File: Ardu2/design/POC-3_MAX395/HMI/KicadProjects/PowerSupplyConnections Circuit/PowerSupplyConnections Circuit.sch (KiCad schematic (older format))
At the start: 16 parts, among them P1 GND, P2 GND, P3 Wiper, P4 Wiper, P5 3.3v, P6 5v

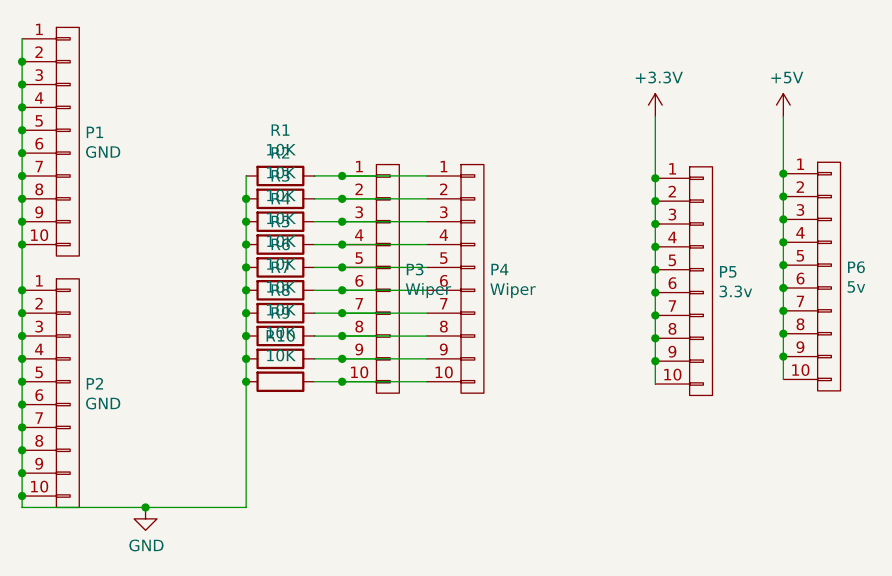
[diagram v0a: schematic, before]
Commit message: created a new peripherals PCB
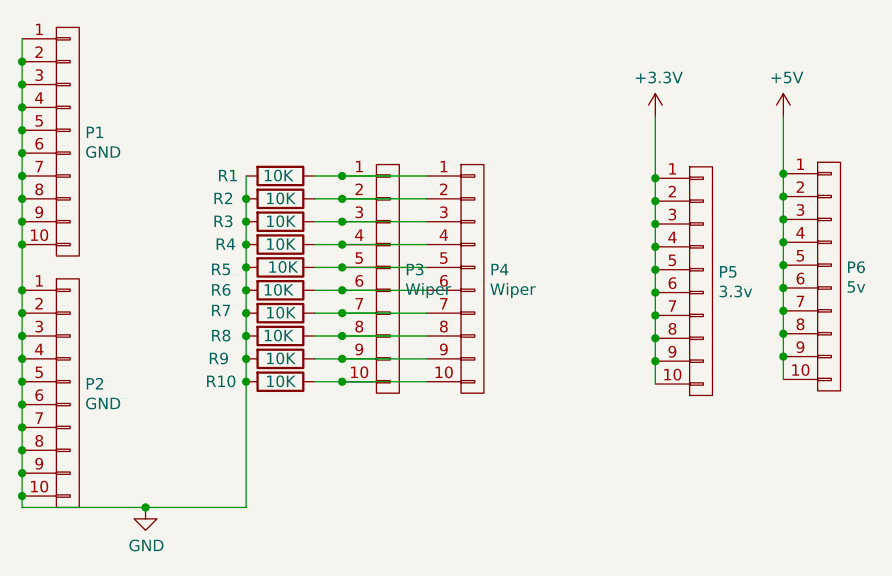
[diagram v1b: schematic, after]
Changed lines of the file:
@@
 LIBS:contrib
 LIBS:valves
+LIBS:PowerSupplyConnections Circuit-cache
 EELAYER 25 0
 EELAYER END
@@
 U 1 1 574B59D1
 P 3570 2660
-F 0 "R1" V 3371 2660 50  0000 C CNN
-F 1 "10K" V 3457 2660 50  0000 C CNN
+F 0 "R1" V 3570 2430 50  0000 C CNN
+F 1 "10K" V 3570 2650 50  0000 C CNN
 F 2 "Resistors_ThroughHole:Resistor_Horizontal_RM10mm" V 3500 2660 50  0001 C CNN
 F 3 "" H 3570 2660 50  0000 C CNN
@@
 U 1 1 574B5BBD
 P 3570 2760
-F 0 "R2" V 3371 2760 50  0000 C CNN
-F 1 "10K" V 3457 2760 50  0000 C CNN
+F 0 "R2" V 3570 2510 50  0000 C CNN
+F 1 "10K" V 3570 2760 50  0000 C CNN
 F 2 "Resistors_ThroughHole:Resistor_Horizontal_RM10mm" V 3500 2760 50  0001 C CNN
 F 3 "" H 3570 2760 50  0000 C CNN
@@
 U 1 1 574B5C0B
 P 3570 2860
-F 0 "R3" V 3371 2860 50  0000 C CNN
-F 1 "10K" V 3457 2860 50  0000 C CNN
+F 0 "R3" V 3570 2610 50  0000 C CNN
+F 1 "10K" V 3570 2860 50  0000 C CNN
 F 2 "Resistors_ThroughHole:Resistor_Horizontal_RM10mm" V 3500 2860 50  0001 C CNN
 F 3 "" H 3570 2860 50  0000 C CNN
@@
 U 1 1 574B5E4B
 P 3570 2960
-F 0 "R4" V 3371 2960 50  0000 C CNN
-F 1 "10K" V 3457 2960 50  0000 C CNN
+F 0 "R4" V 3570 2720 50  0000 C CNN
+F 1 "10K" V 3570 2960 50  0000 C CNN
 F 2 "Resistors_ThroughHole:Resistor_Horizontal_RM10mm" V 3500 2960 50  0001 C CNN
 F 3 "" H 3570 2960 50  0000 C CNN
@@
 U 1 1 574B5EAF
 P 3570 3060
-F 0 "R5" V 3371 3060 50  0000 C CNN
-F 1 "10K" V 3457 3060 50  0000 C CNN
+F 0 "R5" V 3580 2800 50  0000 C CNN
+F 1 "10K" V 3570 3070 50  0000 C CNN
 F 2 "Resistors_ThroughHole:Resistor_Horizontal_RM10mm" V 3500 3060 50  0001 C CNN
 F 3 "" H 3570 3060 50  0000 C CNN
@@
 U 1 1 574B5F1A
 P 3570 3160
-F 0 "R6" V 3371 3160 50  0000 C CNN
-F 1 "10K" V 3457 3160 50  0000 C CNN
+F 0 "R6" V 3570 2900 50  0000 C CNN
+F 1 "10K" V 3570 3150 50  0000 C CNN
 F 2 "Resistors_ThroughHole:Resistor_Horizontal_RM10mm" V 3500 3160 50  0001 C CNN
 F 3 "" H 3570 3160 50  0000 C CNN
@@
 U 1 1 574B5F6A
 P 3570 3260
-F 0 "R7" V 3371 3260 50  0000 C CNN
-F 1 "10K" V 3457 3260 50  0000 C CNN
+F 0 "R7" V 3560 3000 50  0000 C CNN
+F 1 "10K" V 3570 3260 50  0000 C CNN
 F 2 "Resistors_ThroughHole:Resistor_Horizontal_RM10mm" V 3500 3260 50  0001 C CNN
 F 3 "" H 3570 3260 50  0000 C CNN
@@
 U 1 1 574B5FC3
 P 3570 3360
-F 0 "R8" V 3371 3360 50  0000 C CNN
-F 1 "10K" V 3457 3360 50  0000 C CNN
+F 0 "R8" V 3570 3100 50  0000 C CNN
+F 1 "10K" V 3570 3350 50  0000 C CNN
 F 2 "Resistors_ThroughHole:Resistor_Horizontal_RM10mm" V 3500 3360 50  0001 C CNN
 F 3 "" H 3570 3360 50  0000 C CNN
@@
 U 1 1 574B6025
 P 3570 3460
-F 0 "R9" V 3371 3460 50  0000 C CNN
-F 1 "10K" V 3457 3460 50  0000 C CNN
+F 0 "R9" V 3570 3190 50  0000 C CNN
+F 1 "10K" V 3570 3460 50  0000 C CNN
 F 2 "Resistors_ThroughHole:Resistor_Horizontal_RM10mm" V 3500 3460 50  0001 C CNN
 F 3 "" H 3570 3460 50  0000 C CNN
@@
 U 1 1 574B607E
 P 3570 3560
-F 0 "R10" V 3371 3560 50  0000 C CNN
-F 1 "10K" V 3457 3560 50  0000 C CNN
+F 0 "R10" V 3570 3300 50  0000 C CNN
+F 1 "10K" V 3570 3560 50  0000 C CNN
 F 2 "Resistors_ThroughHole:Resistor_Horizontal_RM10mm" V 3500 3560 50  0001 C CNN
 F 3 "" H 3570 3560 50  0000 C CNN
